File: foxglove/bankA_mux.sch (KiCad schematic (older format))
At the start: 5 parts, among them U10 SHIFTER, U9 74HC4051

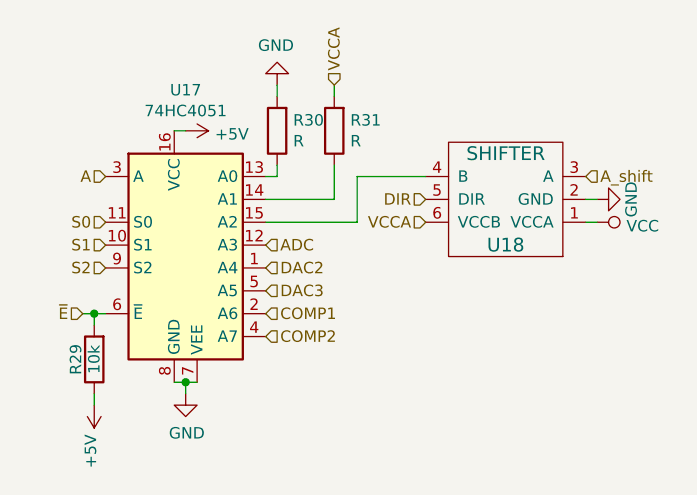
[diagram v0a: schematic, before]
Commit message: Continued work on Foxglove schematic (added bypass caps, selected footprints, etc.). Placed parts on PCB.
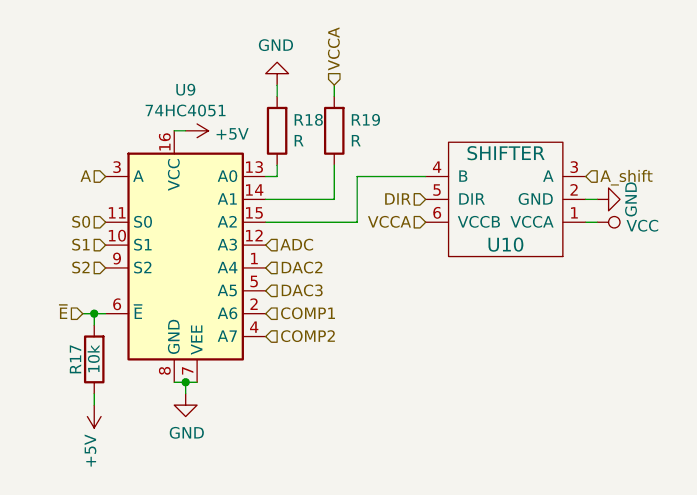
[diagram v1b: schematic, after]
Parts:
- U9: footprint Package_DFN_QFN:VQFN-28-1EP_4x5mm_P0.5mm_EP2.55x3.55mm_ThermalVias -> Package_TO_SOT_SMD:SOT-763-1
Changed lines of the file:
@@
 AR Path="/5D1A4680/5CF3E254" Ref="U21"  Part="1"
 AR Path="/5D1A4696/5CF3E254" Ref="U23"  Part="1"
-F 0 "U17" H 4100 3428 50  0000 C CNN
+F 0 "U9" H 4100 3428 50  0000 C CNN
 F 1 "74HC4051" H 4100 3337 50  0000 C CNN
-F 2 "Package_DFN_QFN:VQFN-28-1EP_4x5mm_P0.5mm_EP2.55x3.55mm_ThermalVias" H 4050 2350 50  0001 C CNN
+F 2 "Package_TO_SOT_SMD:SOT-763-1" H 4050 2350 50  0001 C CNN
 F 3 "http://www.ti.com/lit/ds/symlink/cd74hc4051.pdf" H 4050 2350 50  0001 C CNN
 F 4 "Nexperia USA Inc." H 4050 2750 50  0001 C CNN "Manufacturer"
@@
 AR Path="/5D1A4680/5CF3E25C" Ref="#PWR0180"  Part="1"
 AR Path="/5D1A4696/5CF3E25C" Ref="#PWR0186"  Part="1"
-F 0 "#PWR0168" H 4100 2100 50  0001 C CNN
+F 0 "#PWR0144" H 4100 2100 50  0001 C CNN
 F 1 "+5V" V 4115 2378 50  0000 L CNN
 F 2 "" H 4100 2250 50  0001 C CNN
@@
 AR Path="/5D1A4680/5CF3E263" Ref="#PWR0181"  Part="1"
 AR Path="/5D1A4696/5CF3E263" Ref="#PWR0187"  Part="1"
-F 0 "#PWR0169" H 4100 3150 50  0001 C CNN
+F 0 "#PWR0145" H 4100 3150 50  0001 C CNN
 F 1 "GND" H 4105 3227 50  0000 C CNN
 F 2 "" H 4100 3400 50  0001 C CNN
@@
 AR Path="/5D1A4680/5CF3E26E" Ref="R36"  Part="1"
 AR Path="/5D1A4696/5CF3E26E" Ref="R39"  Part="1"
-F 0 "R30" H 4430 2204 50  0000 R CNN
+F 0 "R18" H 4430 2204 50  0000 R CNN
 F 1 "R" H 4430 2295 50  0000 R CNN
 F 2 "gsg-modules:0402" V 4430 2250 50  0001 C CNN
@@
 AR Path="/5D1A4680/5CF3E275" Ref="R37"  Part="1"
 AR Path="/5D1A4696/5CF3E275" Ref="R40"  Part="1"
-F 0 "R31" H 4680 2204 50  0000 R CNN
+F 0 "R19" H 4680 2204 50  0000 R CNN
 F 1 "R" H 4680 2295 50  0000 R CNN
 F 2 "gsg-modules:0402" V 4680 2250 50  0001 C CNN
@@
 AR Path="/5D1A4680/5CF3E282" Ref="#PWR0182"  Part="1"
 AR Path="/5D1A4696/5CF3E282" Ref="#PWR0188"  Part="1"
-F 0 "#PWR0170" H 4500 1800 50  0001 C CNN
+F 0 "#PWR0146" H 4500 1800 50  0001 C CNN
 F 1 "GND" H 4505 1877 50  0000 C CNN
 F 2 "" H 4500 2050 50  0001 C CNN
@@
 AR Path="/5D1A4680/5CF3E28C" Ref="U22"  Part="1"
 AR Path="/5D1A4696/5CF3E28C" Ref="U24"  Part="1"
-F 0 "U18" H 5500 2750 60  0000 C CNN
+F 0 "U10" H 5500 2750 60  0000 C CNN
 F 1 "SHIFTER" H 5500 2350 60  0000 C CNN
 F 2 "gsg-modules:SOT363" H 5500 2550 60  0001 C CNN
@@
 AR Path="/5D1A4680/5CF3E293" Ref="#PWR0183"  Part="1"
 AR Path="/5D1A4696/5CF3E293" Ref="#PWR0189"  Part="1"
-F 0 "#PWR0171" H 5900 2300 50  0001 C CNN
+F 0 "#PWR0147" H 5900 2300 50  0001 C CNN
 F 1 "GND" H 5900 2400 50  0000 C CNN
 F 2 "" H 5900 2550 60  0000 C CNN
@@
 AR Path="/5D1A4680/5CF3E2A6" Ref="R35"  Part="1"
 AR Path="/5D1A4696/5CF3E2A6" Ref="R38"  Part="1"
-F 0 "R29" V 3780 3250 50  0000 C CNN
+F 0 "R17" V 3780 3250 50  0000 C CNN
 F 1 "10k" V 3700 3250 50  0000 C CNN
 F 2 "gsg-modules:0402" V 3630 3250 50  0001 C CNN
@@
 AR Path="/5D1A4680/5CF3E2B2" Ref="#PWR0184"  Part="1"
 AR Path="/5D1A4696/5CF3E2B2" Ref="#PWR0190"  Part="1"
-F 0 "#PWR0172" H 3700 3300 50  0001 C CNN
+F 0 "#PWR0148" H 3700 3300 50  0001 C CNN
 F 1 "+5V" V 3715 3578 50  0000 L CNN
 F 2 "" H 3700 3450 50  0001 C CNN
@@
 AR Path="/5D1A4680/5CF3E2B8" Ref="#PWR0185"  Part="1"
 AR Path="/5D1A4696/5CF3E2B8" Ref="#PWR0191"  Part="1"
-F 0 "#PWR0173" H 5900 2500 50  0001 C CNN
+F 0 "#PWR0149" H 5900 2500 50  0001 C CNN
 F 1 "VCC" V 5917 2778 50  0000 L CNN
 F 2 "" H 5900 2650 50  0001 C CNN

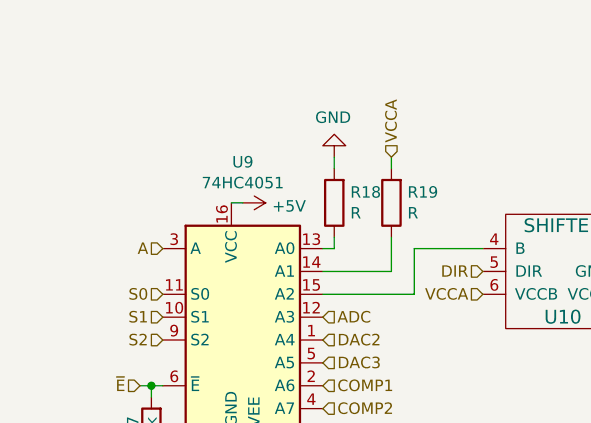
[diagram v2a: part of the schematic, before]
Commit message: Added design notes
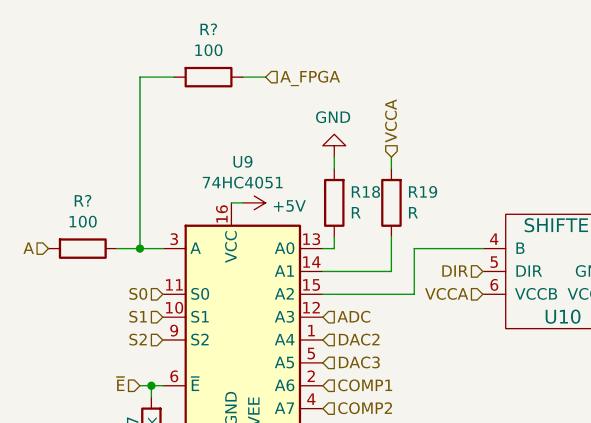
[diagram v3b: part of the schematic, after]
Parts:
- added R? (x2): 100, symbol Device:R
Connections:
- net A: now also R?.2; no longer U9.3 (A)
- new net: R?.1, R?.2, U9.3 (A)
- new net A_FPGA: R?.1
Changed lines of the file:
@@
 F 1 "74HC4051" H 4100 3337 50  0000 C CNN
 F 2 "Package_TO_SOT_SMD:SOT-763-1" H 4050 2350 50  0001 C CNN
-F 3 "http://www.ti.com/lit/ds/symlink/cd74hc4051.pdf" H 4050 2350 50  0001 C CNN
+F 3 "" H 4050 2350 50  0001 C CNN
 F 4 "Nexperia USA Inc." H 4050 2750 50  0001 C CNN "Manufacturer"
 F 5 "74HC4051BQ,115 " H 4050 2750 50  0001 C CNN "Part Number"
@@
 AR Path="/5D1A4680/5CF3E25C" Ref="#PWR0180"  Part="1"
 AR Path="/5D1A4696/5CF3E25C" Ref="#PWR0186"  Part="1"
-F 0 "#PWR0186" H 4100 2100 50  0001 C CNN
+F 0 "#PWR0144" H 4100 2100 50  0001 C CNN
 F 1 "+5V" V 4115 2378 50  0000 L CNN
 F 2 "" H 4100 2250 50  0001 C CNN
@@
 AR Path="/5D1A4680/5CF3E263" Ref="#PWR0181"  Part="1"
 AR Path="/5D1A4696/5CF3E263" Ref="#PWR0187"  Part="1"
-F 0 "#PWR0187" H 4100 3150 50  0001 C CNN
+F 0 "#PWR0145" H 4100 3150 50  0001 C CNN
 F 1 "GND" H 4105 3227 50  0000 C CNN
 F 2 "" H 4100 3400 50  0001 C CNN
@@
 AR Path="/5D1A4680/5CF3E282" Ref="#PWR0182"  Part="1"
 AR Path="/5D1A4696/5CF3E282" Ref="#PWR0188"  Part="1"
-F 0 "#PWR0188" H 4500 1800 50  0001 C CNN
+F 0 "#PWR0146" H 4500 1800 50  0001 C CNN
 F 1 "GND" H 4505 1877 50  0000 C CNN
 F 2 "" H 4500 2050 50  0001 C CNN
@@
 AR Path="/5D1A4680/5CF3E293" Ref="#PWR0183"  Part="1"
 AR Path="/5D1A4696/5CF3E293" Ref="#PWR0189"  Part="1"
-F 0 "#PWR0189" H 5900 2300 50  0001 C CNN
+F 0 "#PWR0147" H 5900 2300 50  0001 C CNN
 F 1 "GND" H 5900 2400 50  0000 C CNN
 F 2 "" H 5900 2550 60  0000 C CNN
@@
 AR Path="/5D1A4680/5CF3E2B2" Ref="#PWR0184"  Part="1"
 AR Path="/5D1A4696/5CF3E2B2" Ref="#PWR0190"  Part="1"
-F 0 "#PWR0190" H 3700 3300 50  0001 C CNN
+F 0 "#PWR0148" H 3700 3300 50  0001 C CNN
 F 1 "+5V" V 3715 3578 50  0000 L CNN
 F 2 "" H 3700 3450 50  0001 C CNN
@@
 AR Path="/5D1A4680/5CF3E2B8" Ref="#PWR0185"  Part="1"
 AR Path="/5D1A4696/5CF3E2B8" Ref="#PWR0191"  Part="1"
-F 0 "#PWR0191" H 5900 2500 50  0001 C CNN
+F 0 "#PWR0149" H 5900 2500 50  0001 C CNN
 F 1 "VCC" V 5917 2778 50  0000 L CNN
 F 2 "" H 5900 2650 50  0001 C CNN
@@
 Text HLabel 5150 2550 0    50   Input ~ 0
 DIR
-Text HLabel 3750 2450 0    50   Input ~ 0
+Text HLabel 3250 2450 0    50   Input ~ 0
 A
 Text HLabel 5850 2450 2    50   Input ~ 0
@@
 Text HLabel 4450 3150 2    50   Input ~ 0
 COMP2
+$Comp
+L Device:R R?
+U 1 1 5CB0C423
+P 3400 2450
+AR Path="/5CF421CD/5CB0C423" Ref="R?"  Part="1"
+AR Path="/5D1A4654/5CB0C423" Ref="R?"  Part="1"
+AR Path="/5D1A4680/5CB0C423" Ref="R?"  Part="1"
+AR Path="/5D1A4696/5CB0C423" Ref="R?"  Part="1"
+F 0 "R?" V 3193 2450 50  0000 C CNN
+F 1 "100" V 3284 2450 50  0000 C CNN
+F 2 "" V 3330 2450 50  0001 C CNN
+F 3 "~" H 3400 2450 50  0001 C CNN
+	1    3400 2450
+	0    1    1    0
+$EndComp
+Wire Wire Line
+	3550 2450 3650 2450
+Wire Wire Line
+	3650 2450 3650 1700
+Wire Wire Line
+	3650 1700 3800 1700
+Connection ~ 3650 2450
+Wire Wire Line
+	3650 2450 3750 2450
+$Comp
+L Device:R R?
+U 1 1 5CB1040C
+P 3950 1700
+AR Path="/5CF421CD/5CB1040C" Ref="R?"  Part="1"
+AR Path="/5D1A4654/5CB1040C" Ref="R?"  Part="1"
+AR Path="/5D1A4680/5CB1040C" Ref="R?"  Part="1"
+AR Path="/5D1A4696/5CB1040C" Ref="R?"  Part="1"
+F 0 "R?" V 3743 1700 50  0000 C CNN
+F 1 "100" V 3834 1700 50  0000 C CNN
+F 2 "" V 3880 1700 50  0001 C CNN
+F 3 "~" H 3950 1700 50  0001 C CNN
+	1    3950 1700
+	0    1    1    0
+$EndComp
+Wire Wire Line
+	4100 1700 4200 1700
+Text HLabel 4200 1700 2    50   Input ~ 0
+A_FPGA
 $EndSCHEMATC

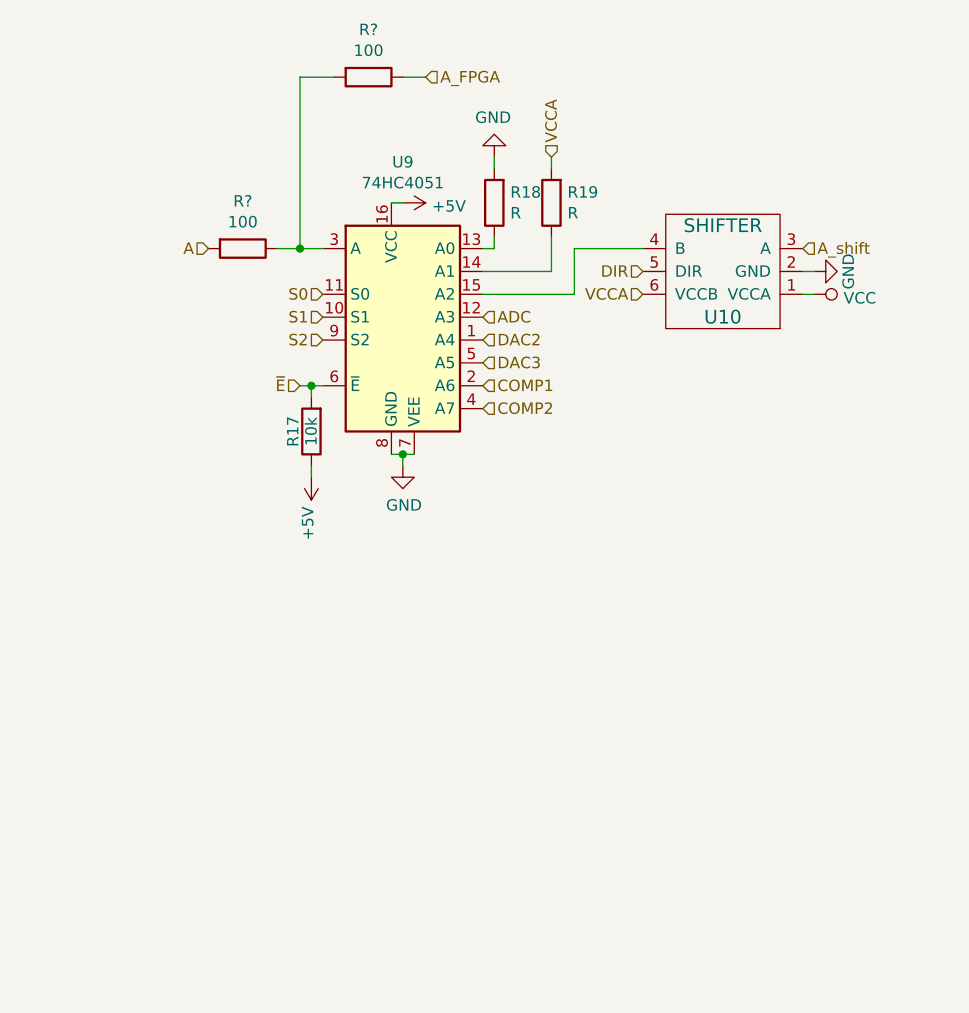
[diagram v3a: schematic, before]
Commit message: Added switch for pull-up/down in parallel with ADC
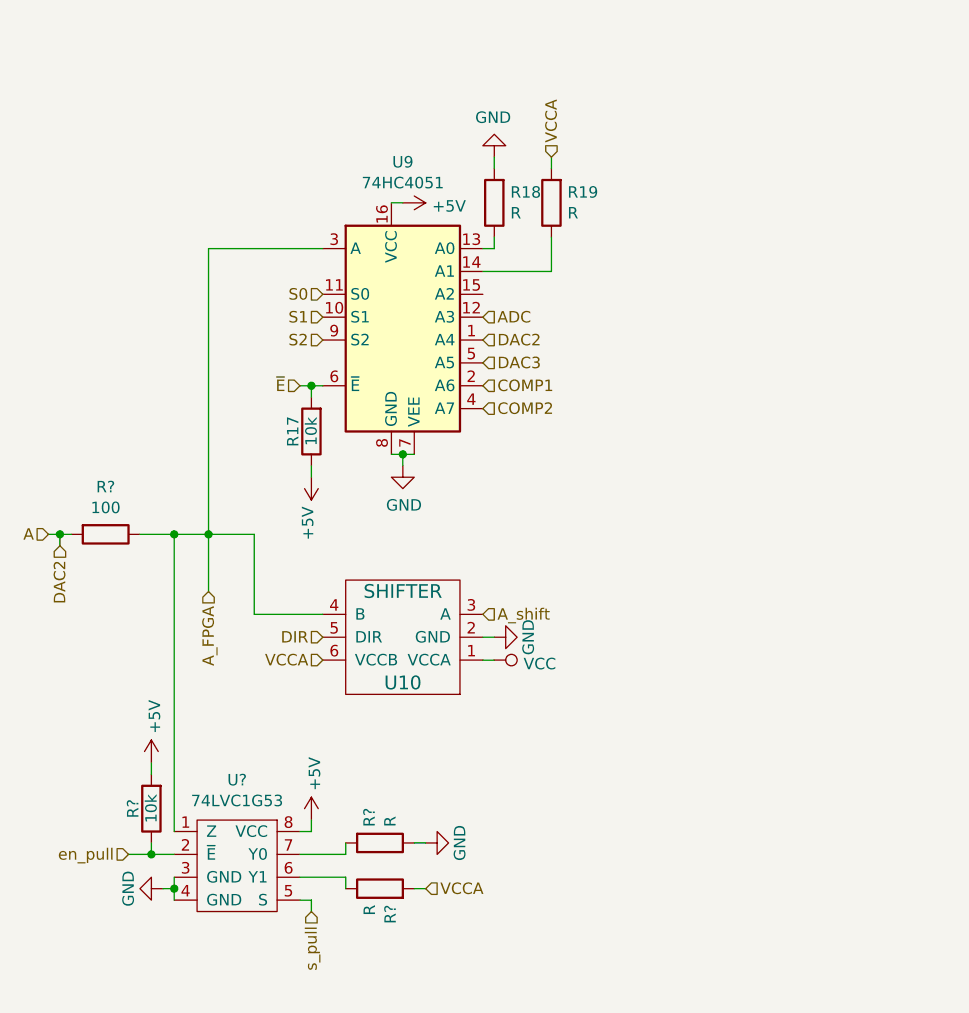
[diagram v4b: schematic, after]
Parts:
- removed R?: 100, symbol Device:R
- added R? (x2): R, gsg-modules:0402, symbol Device:R
- added R?: 10k, gsg-modules:0402, symbol Device:R
- added U?: 74LVC1G53, symbol gsg-symbols:74LVC1G53
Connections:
- net DAC2 is gone; now on net A: U9.1 (A4)
- net +5V: now also R?.2, U?.8 (VCC)
- net A_FPGA: now also R?.1, U10.4 (B), U9.3 (A), U?.1 (Z)
- net GND: now also R?.1, U?.3 (GND), U?.4 (GND)
- net VCCA: now also R?.2
- net at U9.15 (A2): no longer U10.4 (B)
- new net: R?.1, U?.6 (Y1)
- new net: R?.2, U?.7 (Y0)
- new net en_pull: R?.1, U?.2 (~E~)
- new net s_pull: U?.5 (S)
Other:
- moved on the sheet: R?, U10

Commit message: added design notes
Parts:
- R?: value 100 -> 0
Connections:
- net ADC: now also U?.1 (Z)
- net A_FPGA: no longer U?.1 (Z)
- net COMP2: no longer names the net of U9.4 (A7)
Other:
- note added: "add direct\nconnections to gnd and vcc"
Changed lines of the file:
@@
 Text HLabel 4450 3050 2    50   Input ~ 0
 COMP1
-Text HLabel 4450 3150 2    50   Input ~ 0
-COMP2
 $Comp
 L Device:R R?
@@
 AR Path="/5D1A4696/5CB0C423" Ref="R?"  Part="1"
 F 0 "R?" V 2593 3700 50  0000 C CNN
-F 1 "100" V 2684 3700 50  0000 C CNN
+F 1 "0" V 2684 3700 50  0000 C CNN
 F 2 "" V 2730 3700 50  0001 C CNN
 F 3 "~" H 2800 3700 50  0001 C CNN
@@
 Text HLabel 3250 3950 3    50   Input ~ 0
 A_FPGA
-Wire Wire Line
-	2950 3700 3100 3700
 Wire Wire Line
 	3250 3700 3250 2450
@@
 $EndComp
 Wire Wire Line
-	3100 3700 3100 5000
-Connection ~ 3100 3700
-Wire Wire Line
-	3100 3700 3250 3700
-Wire Wire Line
 	3650 5300 3700 5300
 Wire Wire Line
@@
 Wire Wire Line
 	3000 4700 3000 4750
+Wire Wire Line
+	2950 3700 3250 3700
+Text HLabel 3150 4650 2    50   Input ~ 0
+ADC
+Wire Wire Line
+	3150 4650 3100 4650
+Wire Wire Line
+	3100 4650 3100 5000
+Text Notes 4900 2800 0    50   ~ 0
+add direct\nconnections to gnd and vcc
 $EndSCHEMATC

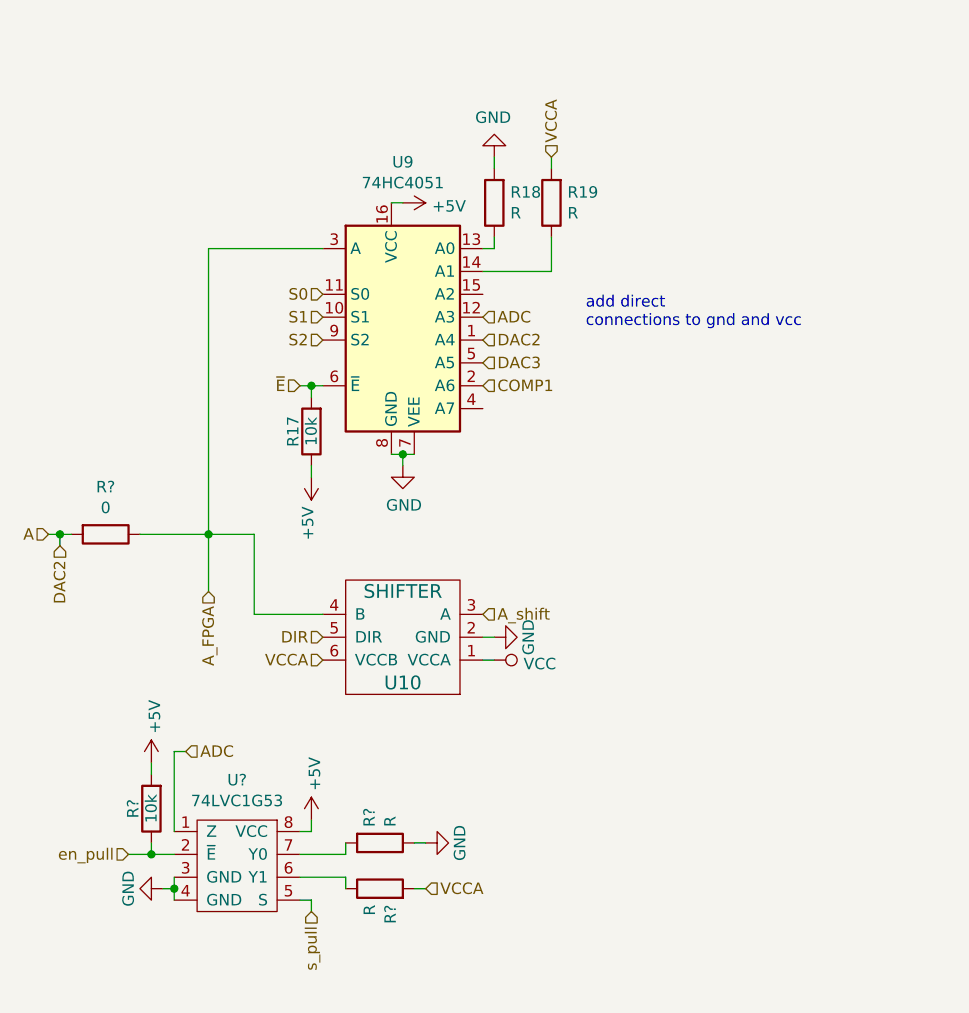
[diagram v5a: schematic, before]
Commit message: Routed FPGA power and JTAG connections
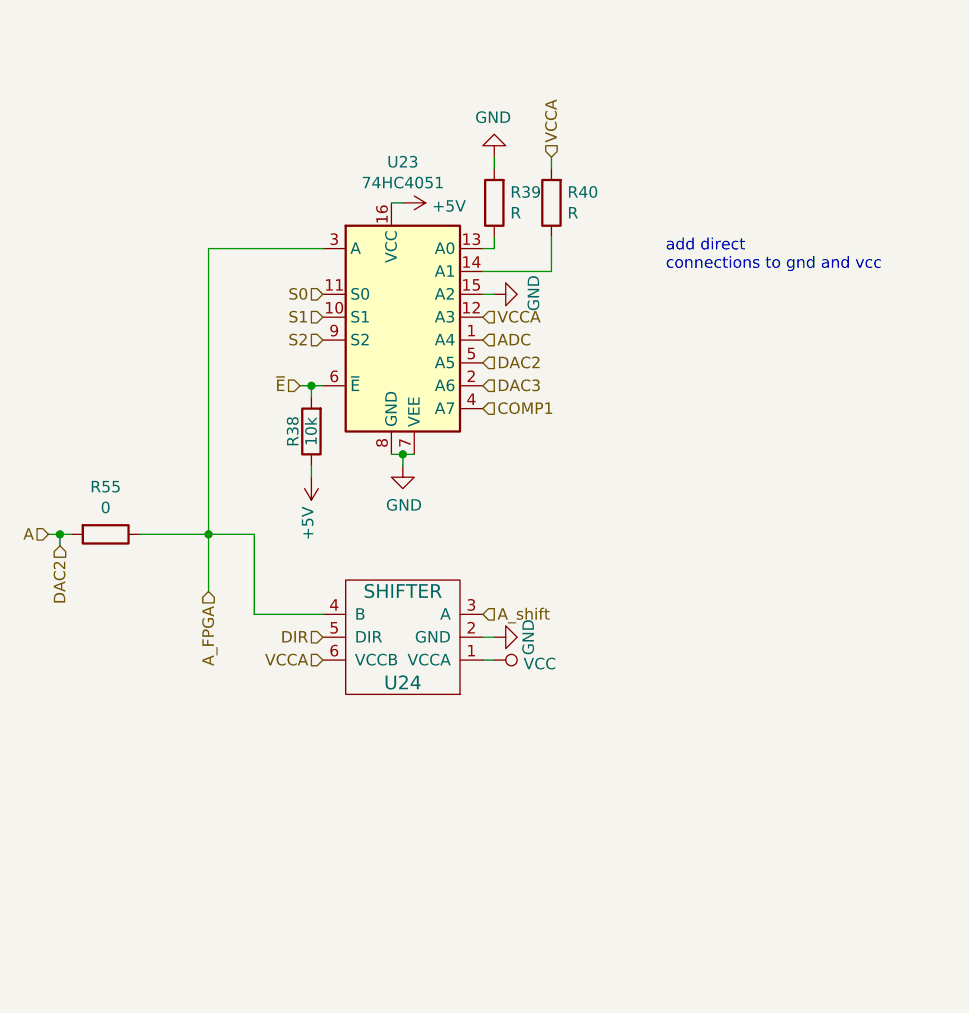
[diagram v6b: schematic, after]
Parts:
- removed R? (x2): R, gsg-modules:0402, symbol Device:R
- removed R?: 10k, gsg-modules:0402, symbol Device:R
- removed U?: 74LVC1G53, symbol gsg-symbols:74LVC1G53
- R48: renamed from R?; footprint (none) -> gsg-modules:0402
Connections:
- net A: now also U9.5 (A5); no longer U9.1 (A4)
- net ADC: now also U9.1 (A4); no longer U9.12 (A3)
- net COMP1: now also U9.4 (A7); no longer U9.2 (A6)
- net DAC3: now also U9.2 (A6); no longer U9.5 (A5)
- net GND: now also U9.15 (A2)
- net VCCA: now also U9.12 (A3)
